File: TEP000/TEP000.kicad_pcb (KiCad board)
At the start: 2 copper layers, 45 x 55 mm, 35 parts, among them J1 SMA, J2 Molex, U1 LT6003HS5#TRMPBF, U2 MAX889TESA+, U3 XC6209F332MR-G, U4 XC6902N331MR-G

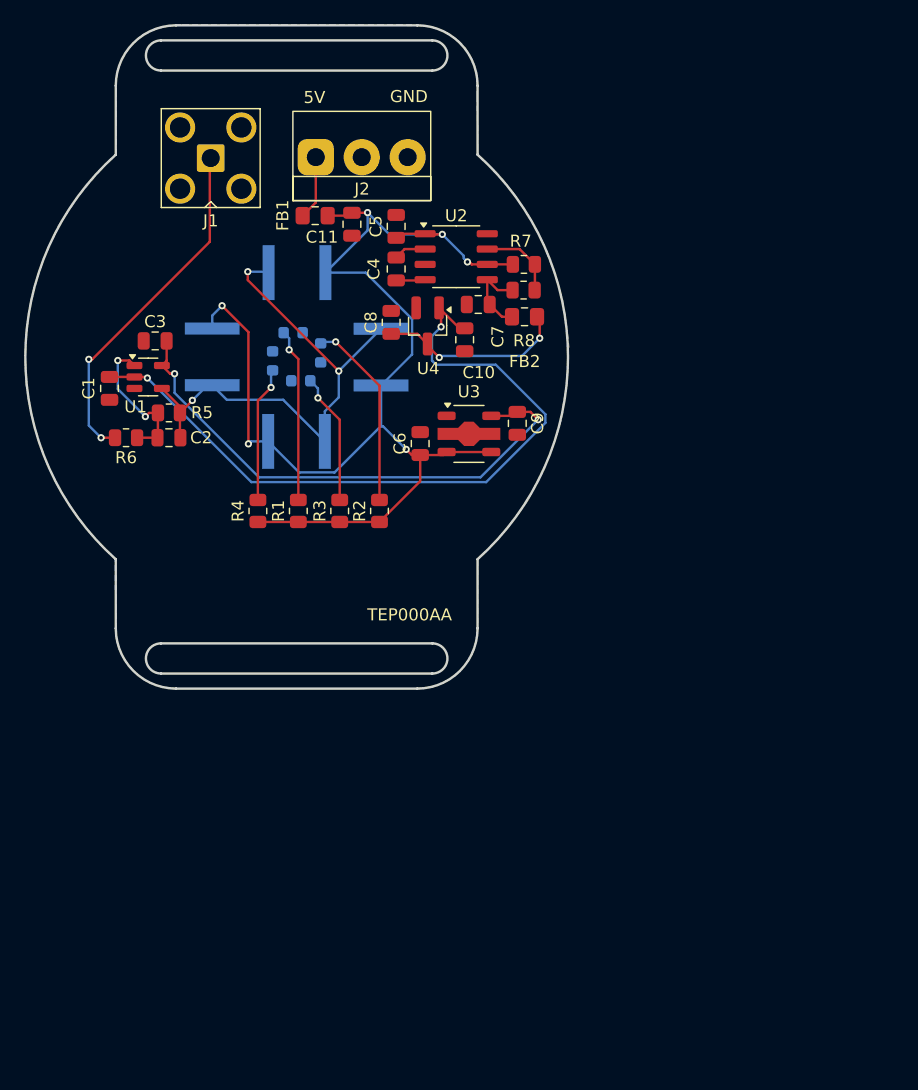
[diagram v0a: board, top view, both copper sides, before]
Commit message: TEP000AB
Added buck-boost converters, MCU and integrator bleed circuit.
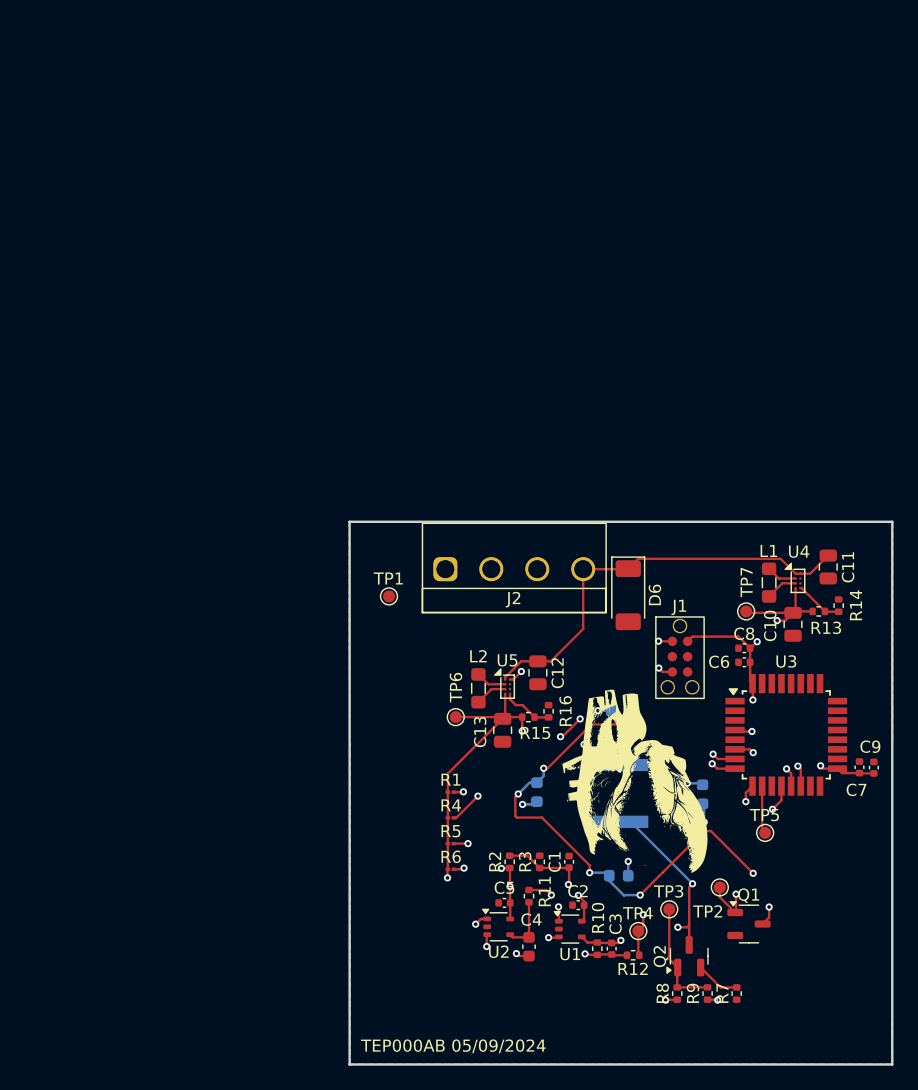
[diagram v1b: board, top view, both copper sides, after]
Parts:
- removed D7, D8: TEMD5510FX01, MyFootPrints:TEMD5510FX01
- removed FB1, FB2: MMZ2012Y600BT000, Capacitor_SMD:C_0805_2012Metric_Pad1.18x1.45mm_HandSolder
- added C12: 22uF, Capacitor_SMD:C_0805_2012Metric, F.Cu at (154.4, 103.1)
- added C13: 47uF, Capacitor_SMD:C_0805_2012Metric, F.Cu at (151.5, 107.9)
- added G***: LOGO, LOGO, F.Cu at (163.1, 114.1)
- added L1: 1uH, Inductor_SMD:L_0805_2012Metric_Pad1.05x1.20mm_HandSolder, F.Cu at (173.6, 95.6)
- added L2: 1uH, Inductor_SMD:L_0805_2012Metric_Pad1.05x1.20mm_HandSolder, F.Cu at (149.5, 104.4)
- added Q1: 2N7002k-7, Package_TO_SOT_SMD:SOT-23-3, F.Cu at (171.9, 123.9)
- added Q2: BC849C,125, Package_TO_SOT_SMD:SOT-23, F.Cu at (166.9, 126.6)
- added R10: 1Meg, Resistor_SMD:R_0402_1005Metric, F.Cu at (159.3, 126.0)
- added R11: 1Meg, Resistor_SMD:R_0402_1005Metric, F.Cu at (153.6, 121.6)
- added R12: 100R, Resistor_SMD:R_0402_1005Metric, F.Cu at (162.3, 126.5)
- added R13: 511k, Resistor_SMD:R_0402_1005Metric, F.Cu at (177.7, 98.0)
- added R14: 91k, Resistor_SMD:R_0402_1005Metric, F.Cu at (179.3, 97.5)
- added R15: 511k, Resistor_SMD:R_0402_1005Metric, F.Cu at (153.6, 106.8)
- added R16: 91k, Resistor_SMD:R_0402_1005Metric, F.Cu at (155.3, 106.3)
- added R9: DNM, Resistor_SMD:R_0402_1005Metric, F.Cu at (168.5, 129.7)
- added TP1: GND, TestPoint:TestPoint_Pad_D1.0mm, F.Cu at (142.0, 96.8)
- added TP2: LED_EN, TestPoint:TestPoint_Pad_D1.0mm, F.Cu at (169.5, 120.9)
- added TP3: V_BLEED, TestPoint:TestPoint_Pad_D1.0mm, F.Cu at (165.3, 122.7)
- added TP4: OHR_O, TestPoint:TestPoint_Pad_D1.0mm, F.Cu at (162.7, 124.5)
- added TP5: MCU, TestPoint:TestPoint_Pad_D1.0mm, F.Cu at (173.2, 116.4)
- added TP6: 3V3A, TestPoint:TestPoint_Pad_D1.0mm, F.Cu at (147.6, 106.8)
- added TP7: 3V3A, TestPoint:TestPoint_Pad_D1.0mm, F.Cu at (171.7, 98.0)
- added U5: TPS631011, Package_BGA:Texas_DSBGA-8_0.705x1.468mm_Layout2x4_P0.4mm, F.Cu at (151.9, 104.3)
- C1: footprint Capacitor_SMD:C_0805_2012Metric -> Capacitor_SMD:C_0402_1005Metric
- C10: value 10uF -> 47uF
- C11: value 10uF -> 22uF
- C2: value 160pF -> 0u1; footprint Capacitor_SMD:C_0805_2012Metric -> Capacitor_SMD:C_0402_1005Metric
- C3: value 0u1 -> 160pF; footprint Capacitor_SMD:C_0805_2012Metric -> Capacitor_SMD:C_0402_1005Metric
- C4: value 1uF -> 1u5; footprint Capacitor_SMD:C_0805_2012Metric -> Capacitor_SMD:C_0603_1608Metric
- C5, C6, C7: value 10uF -> 0u1; footprint Capacitor_SMD:C_0805_2012Metric -> Capacitor_SMD:C_0402_1005Metric
- C8, C9: value 10uF -> 1u; footprint Capacitor_SMD:C_0805_2012Metric -> Capacitor_SMD:C_0402_1005Metric
- D6: value TEMD5510FX01 -> fast; footprint MyFootPrints:TEMD5510FX01 -> Diode_SMD:D_SOD-128; moved to F.Cu
- J1: value SMA -> AVR-PDI-6; footprint Connector_Coaxial:SMA_Amphenol_901-143_Horizontal -> MyFootPrints:PDI_AVR_TagConnect
- J2: value Molex -> Conn; footprint MyFootPrints:Screwterminal_3mm81_3pos -> MyFootPrints:3.81mm4PosTerm_2007987
- R1, R4: value 75R -> 15R; footprint Resistor_SMD:R_0805_2012Metric -> Resistor_SMD:R_01005_0402Metric
- R2, R3: value 75R -> 100k; footprint Resistor_SMD:R_0805_2012Metric -> Resistor_SMD:R_0402_1005Metric
- R5: value 1Meg -> 15R; footprint Resistor_SMD:R_0805_2012Metric -> Resistor_SMD:R_01005_0402Metric
- R6: value 100R -> 15R; footprint Resistor_SMD:R_0805_2012Metric -> Resistor_SMD:R_01005_0402Metric
- R7: value 100k -> 100R; footprint Resistor_SMD:R_0805_2012Metric -> Resistor_SMD:R_0402_1005Metric
- R8: value 91k -> 100R; footprint Resistor_SMD:R_0805_2012Metric -> Resistor_SMD:R_0402_1005Metric
- U1: value LT6003HS5#TRMPBF -> MCP6006T-E/LT; footprint Package_TO_SOT_SMD:SOT-23-5 -> Package_TO_SOT_SMD:SOT-353_SC-70-5
- U2: value MAX889TESA+ -> MCP6006T-E/LT; footprint Package_SO:SO-8_3.9x4.9mm_P1.27mm -> Package_TO_SOT_SMD:SOT-353_SC-70-5
- U3: value XC6209F332MR-G -> ATxmega8E5-A; footprint Package_TO_SOT_SMD:SOT-89-5 -> Package_QFP:TQFP-32_7x7mm_P0.8mm
- U4: value XC6902N331MR-G -> TPS631011; footprint Package_TO_SOT_SMD:SOT-23_Handsoldering -> Package_BGA:Texas_DSBGA-8_0.705x1.468mm_Layout2x4_P0.4mm
- moved C3 63.0 mm to (160.5, 126.0), turned to -90 degrees
- moved R7 63.0 mm to (170.9, 129.7), turned to -90 degrees
- moved R8 59.7 mm to (165.9, 129.7), turned to 90 degrees
- moved U1 57.6 mm to (157.1, 124.4)
- moved C4 57.3 mm to (153.6, 125.8), turned to 90 degrees
- moved C5 56.8 mm to (151.6, 122.2), turned to 180 degrees
- moved J1 56.8 mm to (166.2, 101.8)
- moved U2 55.7 mm to (151.1, 124.2)
- moved C1 54.7 mm to (157.0, 118.8), turned to 90 degrees
- moved C2 51.5 mm to (157.7, 122.4)
- moved D4 51.4 mm to (161.1, 119.9), turned to 0 degrees
- moved D5 50.9 mm to (161.3, 113.1), turned to -90 degrees
- moved C7 49.7 mm to (181.1, 110.9), turned to -90 degrees
- moved C11 48.7 mm to (178.5, 94.3), turned to -90 degrees
- moved D3 47.8 mm to (168.0, 113.2), turned to 90 degrees
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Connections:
- C1 pad 1: -3V3 -> Vref
- C10 pad 1: -3V3 -> +3V3
- C11 pad 1: GND -> VDC
- C11 pad 2: +5V -> GND
- C2 pad 1: Net-(D5-A) -> +3.3VA
- C2 pad 2: Net-(C2-Pad2) -> GND
- C3 pad 1: +3V3 -> Net-(D5-A)
- C3 pad 2: GND -> Net-(C3-Pad2)
- C4 pad 1: Net-(U2-CAP+) -> Net-(C4-Pad1)
- C5 pad 1: +5V -> +3.3VA
- C6 pad 1: +5V -> +3V3
- C7 pad 1: Net-(U2-OUT) -> GND
- C7 pad 2: GND -> +3V3
- C8 pad 1: Net-(U4--IN) -> GND
- C8 pad 2: GND -> +3V3
- D1 pad 1: GND -> Net-(D1-K)
- D2 pad 1: GND -> Net-(D1-K)
- D3 pad 1: GND -> Net-(D1-K)
- D4 pad 1: GND -> Net-(D1-K)
- D5 pad 1: +5V -> +3.3VA
- D6 pad 1: +5V -> VDC
- D6 pad 2: Net-(D5-A) -> GND
- J1 pad 1: Net-(J1-In) -> PDI_DATA
- J1 pad 2: GND -> +3V3
- J2 pad 1: Net-(J2-Pin_1) -> GND
- J2 pad 2: unconnected-(J2-Pin_2-Pad2) -> MCU_TX
- J2 pad 3: GND -> MCU_RX
- R1 pad 1: +5V -> +3.3VA
- R2 pad 1: +5V -> +3.3VA
- R2 pad 2: Net-(D2-A) -> Vref
- R3 pad 1: +5V -> Vref
- R3 pad 2: Net-(D3-A) -> GND
- R4 pad 1: +5V -> +3.3VA
- R4 pad 2: Net-(D4-A) -> Net-(D2-A)
- R5 pad 1: Net-(D5-A) -> +3.3VA
- R5 pad 2: Net-(C2-Pad2) -> Net-(D3-A)
- R6 pad 1: Net-(C2-Pad2) -> +3.3VA
- R6 pad 2: Net-(J1-In) -> Net-(D4-A)
- R7 pad 1: Net-(U2-FB) -> Net-(Q2-E)
- R7 pad 2: +5V -> GND
- R8 pad 1: Net-(U2-FB) -> Net-(C4-Pad1)
- R8 pad 2: Net-(U2-OUT) -> Net-(Q2-B)
- U1 pad 1: Net-(C2-Pad2) -> Net-(C3-Pad2)
- U1 pad 2: -3V3 -> GND
- U1 pad 3: GND -> Vref
- U1 pad 5: +3V3 -> +3.3VA
- U2 pad 1: +5V -> Net-(C4-Pad1)
- U2 pad 2: Net-(U2-CAP+) -> GND
- U2 pad 3: GND -> Vref
- U2 pad 5: Net-(U2-OUT) -> +3.3VA
- U3 pad 1: unconnected-(U3-NC-Pad1) -> GND
- U3 pad 2: GND -> unconnected-(U3-PA4-Pad2)
- U3 pad 3: +5V -> unconnected-(U3-PA3-Pad3)
- U3 pad 4: +5V -> DAC
- U3 pad 5: +3V3 -> unconnected-(U3-PA1-Pad5)
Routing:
- net +5V: track 102.1 -> 0.00 mm, vias 6 -> 0
- net -3V3: track 61.3 -> 0.00 mm, vias 2 -> 0
- net +3.3VA: track 0.00 -> 53.2 mm, vias 0 -> 7
- net Net-(D1-K): track 0.00 -> 49.0 mm, vias 0 -> 8
- net MCU_TX: track 0.00 -> 36.3 mm, vias 0 -> 1
- net VDC: track 0.00 -> 35.1 mm
- net MCU_RX: track 0.00 -> 35.1 mm, vias 0 -> 1
- net Net-(J1-In): track 29.2 -> 0.00 mm, vias 2 -> 0
- net DAC: track 0.00 -> 26.5 mm, vias 0 -> 2
- net EN_A: track 0.00 -> 25.8 mm, vias 0 -> 2
- net Net-(C4-Pad1): track 0.00 -> 22.8 mm, vias 0 -> 3
- net OHR_ADC: track 0.00 -> 22.8 mm, vias 0 -> 2
- net Net-(D5-A): track 44.0 -> 23.0 mm
- net Vref: track 0.00 -> 20.5 mm, vias 0 -> 3
- net Net-(U4--IN): track 15.7 -> 0.00 mm, vias 2 -> 0
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- added copper zone on In1.Cu, net GND
- added copper zone on In2.Cu, net GND
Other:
- board size 45 x 55 mm -> 45 x 45 mm
- copper layers 2 -> 4
- board text added: "TEP000AB 05/09/2024"
- board text removed: "5V"
- board text removed: "GND"
- board text removed: "TEP000AA"
